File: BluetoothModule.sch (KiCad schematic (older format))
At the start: 13 parts, among them U2 BM83SM1-00TA

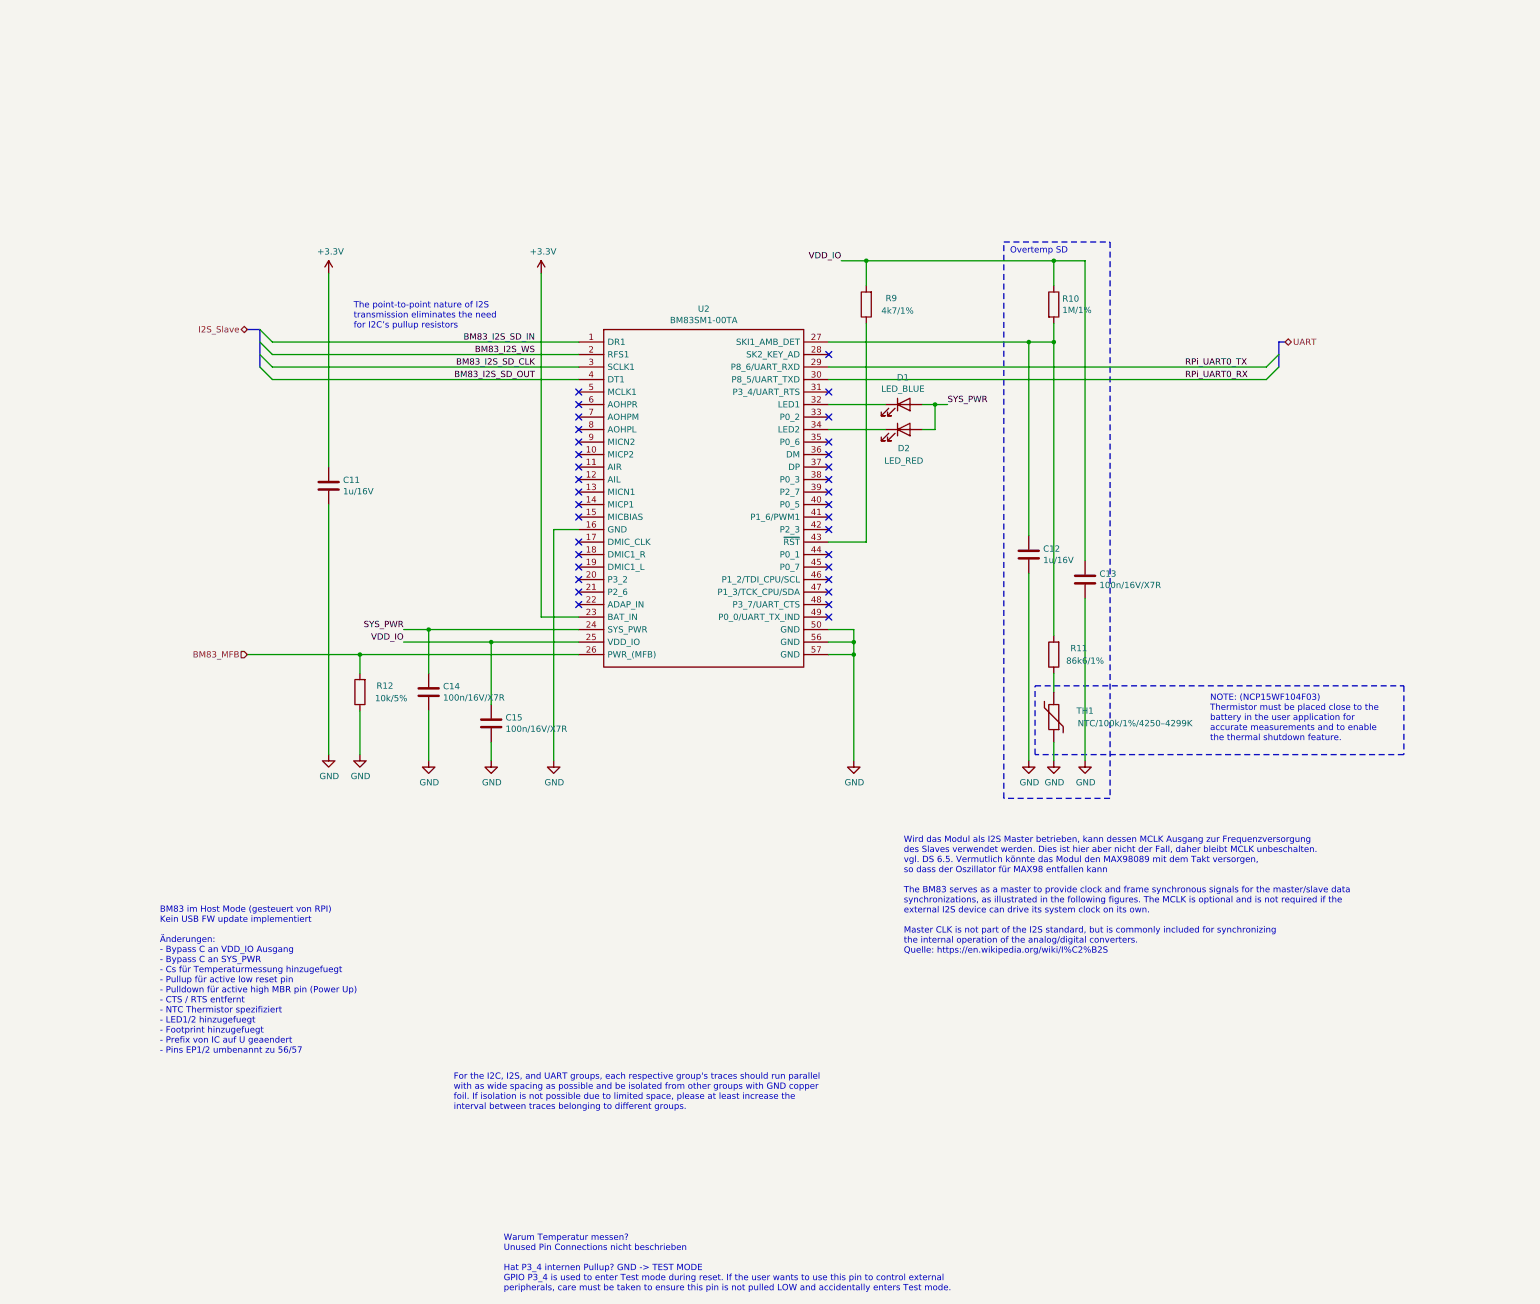
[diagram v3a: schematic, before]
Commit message: - CM3 durch CM4 ersetzt - Spannungsregler für 3,3 und 1,8V entfernt, da nun von CM4 erzeugt - RTC IC getauscht
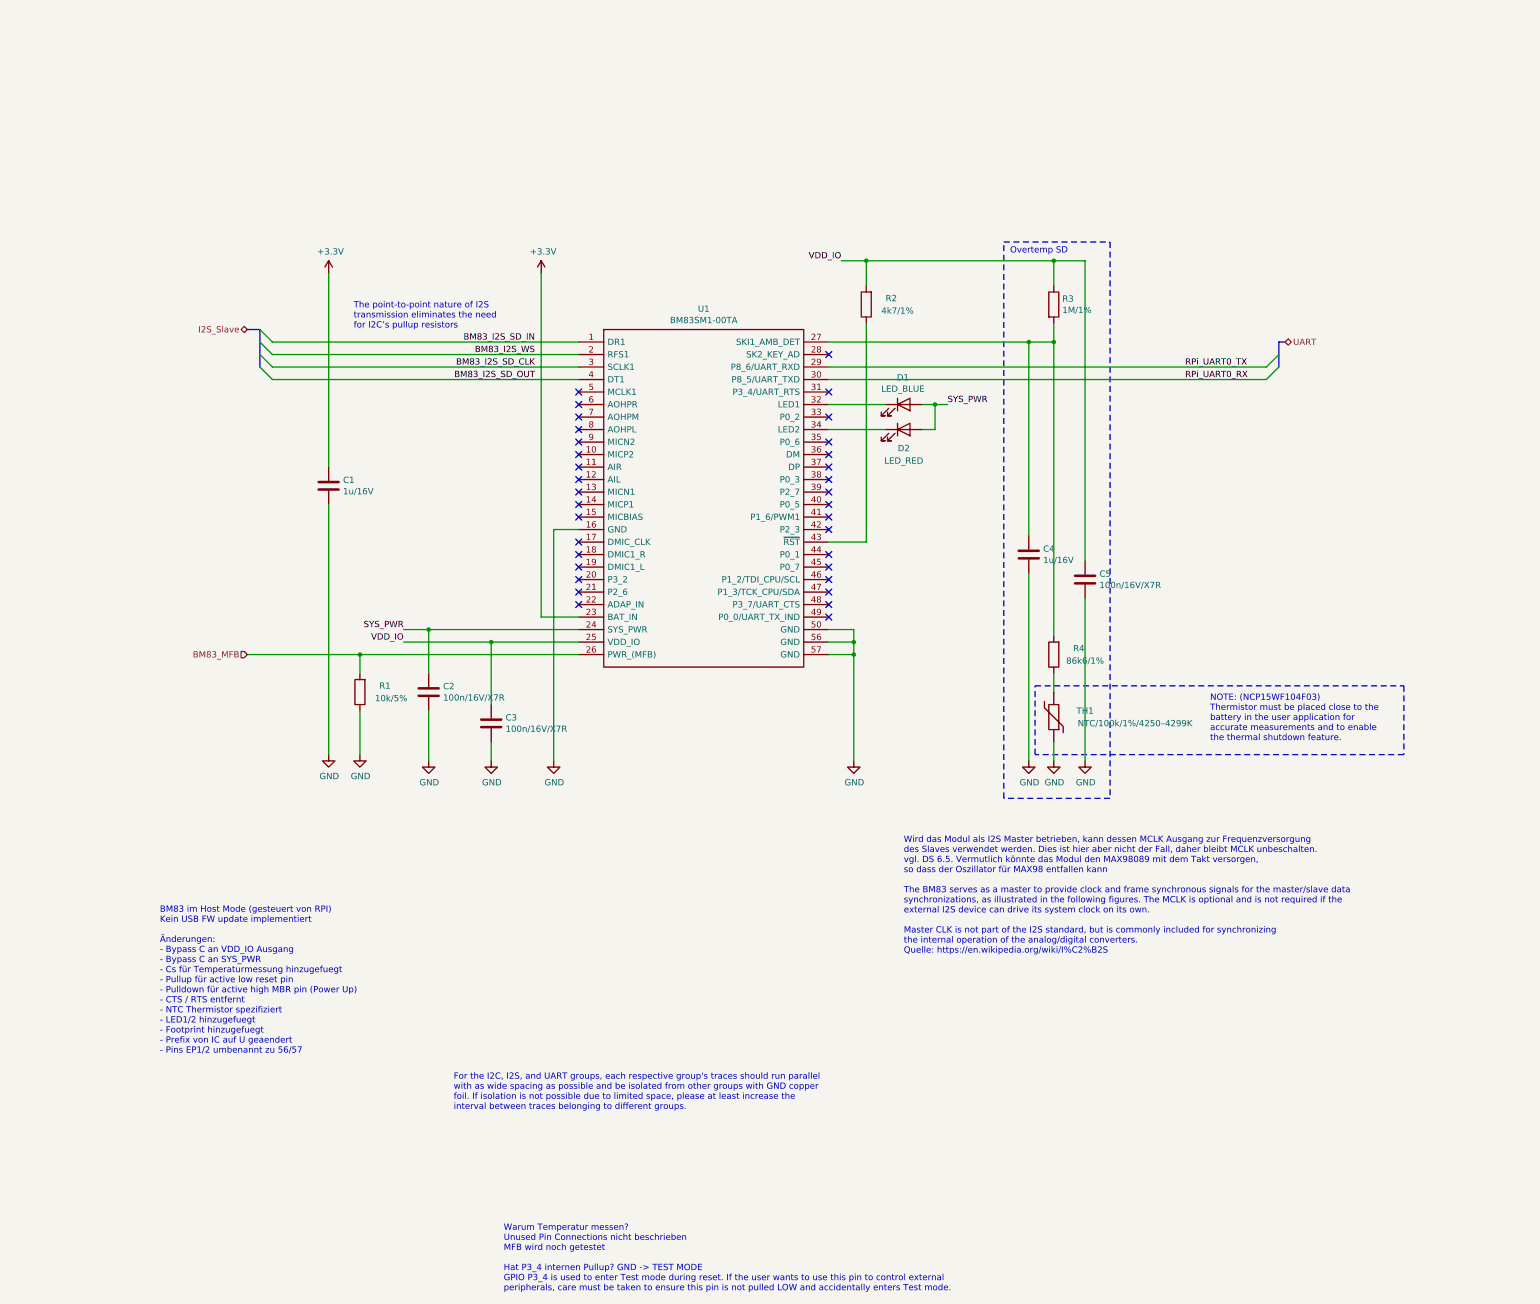
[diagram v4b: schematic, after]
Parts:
- renumbered C11 to C1, C14 to C2, C15 to C3, C12 to C4, C13 to C5, R12 to R1, R9 to R2, R10 to R3, R11 to R4, U2 to U1
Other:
- note added: "Warum Temperatur messen?\nUnused Pin Connections nicht beschrieben\nMFB wird noch getestet\n\nHat P3_4 internen Pullup? GND -> TEST MODE\nGPIO P3_4 is used to enter Test mode during reset. If the user wants to use this pin to control external\nperipherals, care must be taken to ensure this pin is not pulled LOW and accidentally enters Test mode."
- note removed: "Warum Temperatur messen?\nUnused Pin Connections nicht beschrieben\n\nHat P3_4 internen Pullup? GND -> TEST MODE\nGPIO P3_4 is used to enter Test mode during reset. If the user wants to use this pin to control external\nperipherals, care must be taken to ensure this pin is not pulled LOW and accidentally enters Test mode."
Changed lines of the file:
@@
 $Descr A4 11693 8268
 encoding utf-8
-Sheet 3 7
+Sheet 2 8
 Title ""
 Date ""
@@
 BM83_I2S_SD_CLK
 $Comp
-L TeKaDe:BM83SM1-00TA U2
+L TeKaDe:BM83SM1-00TA U1
 U 1 1 620D3641
 P 4400 1450
-F 0 "U2" H 5400 1715 50  0000 C CNN
+F 0 "U1" H 5400 1715 50  0000 C CNN
 F 1 "BM83SM1-00TA" H 5400 1624 50  0000 C CNN
 F 2 "TeKaDe:BM83SM1" H 6250 1550 50  0001 L CNN
@@
 NoConn ~ 4400 3550
 $Comp
-L power:+3.3V #PWR052
+L power:+3.3V #PWR014
 U 1 1 620D3663
 P 4100 900
-F 0 "#PWR052" H 4100 750 50  0001 C CNN
+F 0 "#PWR014" H 4100 750 50  0001 C CNN
 F 1 "+3.3V" H 4115 1073 50  0000 C CNN
 F 2 "" H 4100 900 50  0001 C CNN
@@
 $EndComp
 $Comp
-L Device:C C11
+L Device:C C1
 U 1 1 620D366F
 P 2400 2600
-F 0 "C11" H 2515 2646 50  0000 L CNN
+F 0 "C1" H 2515 2646 50  0000 L CNN
 F 1 "1u/16V" H 2515 2555 50  0000 L CNN
 F 2 "Capacitor_SMD:C_0603_1608Metric" H 2438 2450 50  0001 C CNN
@@
 NoConn ~ 6400 3650
 $Comp
-L power:GND #PWR057
+L power:GND #PWR015
 U 1 1 620E43D7
 P 4200 4800
-F 0 "#PWR057" H 4200 4550 50  0001 C CNN
+F 0 "#PWR015" H 4200 4550 50  0001 C CNN
 F 1 "GND" H 4205 4627 50  0000 C CNN
 F 2 "" H 4200 4800 50  0001 C CNN
@@
 	4200 2950 4400 2950
 $Comp
-L power:GND #PWR058
+L power:GND #PWR016
 U 1 1 620E7F5A
 P 6600 4800
-F 0 "#PWR058" H 6600 4550 50  0001 C CNN
+F 0 "#PWR016" H 6600 4550 50  0001 C CNN
 F 1 "GND" H 6605 4627 50  0000 C CNN
 F 2 "" H 6600 4800 50  0001 C CNN
@@
 $EndComp
 $Comp
-L power:GND #PWR053
+L power:GND #PWR010
 U 1 1 620F327C
 P 2400 4750
-F 0 "#PWR053" H 2400 4500 50  0001 C CNN
+F 0 "#PWR010" H 2400 4500 50  0001 C CNN
 F 1 "GND" H 2405 4577 50  0000 C CNN
 F 2 "" H 2400 4750 50  0001 C CNN
@@
 	2400 4750 2400 2750
 $Comp
-L power:+3.3V #PWR051
+L power:+3.3V #PWR09
 U 1 1 620F6127
 P 2400 900
-F 0 "#PWR051" H 2400 750 50  0001 C CNN
+F 0 "#PWR09" H 2400 750 50  0001 C CNN
 F 1 "+3.3V" H 2415 1073 50  0000 C CNN
 F 2 "" H 2400 900 50  0001 C CNN
@@
 $EndBitmap
 $Comp
-L Device:C C15
+L Device:C C3
 U 1 1 60DA1121
 P 3700 4500
-F 0 "C15" H 3815 4546 50  0000 L CNN
+F 0 "C3" H 3815 4546 50  0000 L CNN
 F 1 "100n/16V/X7R" H 3815 4455 50  0000 L CNN
 F 2 "Capacitor_SMD:C_0603_1608Metric" H 3738 4350 50  0001 C CNN
@@
 $EndComp
 $Comp
-L power:GND #PWR056
+L power:GND #PWR013
 U 1 1 60DA112B
 P 3700 4800
-F 0 "#PWR056" H 3700 4550 50  0001 C CNN
+F 0 "#PWR013" H 3700 4550 50  0001 C CNN
 F 1 "GND" H 3705 4627 50  0000 C CNN
 F 2 "" H 3700 4800 50  0001 C CNN
@@
 	3700 3850 3700 4350
 $Comp
-L Device:C C14
+L Device:C C2
 U 1 1 60DA7A8D
 P 3200 4250
-F 0 "C14" H 3315 4296 50  0000 L CNN
+F 0 "C2" H 3315 4296 50  0000 L CNN
 F 1 "100n/16V/X7R" H 3315 4205 50  0000 L CNN
 F 2 "Capacitor_SMD:C_0603_1608Metric" H 3238 4100 50  0001 C CNN
@@
 $EndComp
 $Comp
-L power:GND #PWR055
+L power:GND #PWR012
 U 1 1 60DA7A97
 P 3200 4800
-F 0 "#PWR055" H 3200 4550 50  0001 C CNN
+F 0 "#PWR012" H 3200 4550 50  0001 C CNN
 F 1 "GND" H 3205 4627 50  0000 C CNN
 F 2 "" H 3200 4800 50  0001 C CNN
@@
 Wird das Modul als I2S Master betrieben, kann dessen MCLK Ausgang zur Frequenzversorgung \ndes Slaves verwendet werden. Dies ist hier aber nicht der Fall, daher bleibt MCLK unbeschalten.\nvgl. DS 6.5. Vermutlich könnte das Modul den MAX98089 mit dem Takt versorgen, \nso dass der Oszillator für MAX98 entfallen kann\n\nThe BM83 serves as a master to provide clock and frame synchronous signals for the master/slave data\nsynchronizations, as illustrated in the following figures. The MCLK is optional and is not required if the\nexternal I2S device can drive its system clock on its own.\n\nMaster CLK is not part of the I2S standard, but is commonly included for synchronizing \nthe internal operation of the analog/digital converters.\nQuelle: https://en.wikipedia.org/wiki/I%C2%B2S
 $Comp
-L Device:R R9
+L Device:R R2
 U 1 1 60DB214B
 P 6700 1150
-F 0 "R9" H 6500 1100 50  0000 C CNN
+F 0 "R2" H 6500 1100 50  0000 C CNN
 F 1 "4k7/1%" H 6450 1200 50  0000 C CNN
 F 2 "Resistor_SMD:R_0603_1608Metric" V 6740 1140 50  0001 C CNN
@@
 Connection ~ 8000 1450
 $Comp
-L power:GND #PWR061
+L power:GND #PWR019
 U 1 1 60DAF699
 P 8450 4800
-F 0 "#PWR061" H 8450 4550 50  0001 C CNN
+F 0 "#PWR019" H 8450 4550 50  0001 C CNN
 F 1 "GND" H 8455 4627 50  0000 C CNN
 F 2 "" H 8450 4800 50  0001 C CNN
@@
 $EndComp
 $Comp
-L power:GND #PWR059
+L power:GND #PWR017
 U 1 1 60DAEFE7
 P 8000 4800
-F 0 "#PWR059" H 8000 4550 50  0001 C CNN
+F 0 "#PWR017" H 8000 4550 50  0001 C CNN
 F 1 "GND" H 8005 4627 50  0000 C CNN
 F 2 "" H 8000 4800 50  0001 C CNN
@@
 $EndComp
 $Comp
-L Device:C C12
+L Device:C C4
 U 1 1 60DAD2BA
 P 8000 3150
-F 0 "C12" H 8115 3196 50  0000 L CNN
+F 0 "C4" H 8115 3196 50  0000 L CNN
 F 1 "1u/16V" H 8115 3105 50  0000 L CNN
 F 2 "Capacitor_SMD:C_0603_1608Metric" H 8038 3000 50  0001 C CNN
@@
 	8200 1450 8200 3800
 $Comp
-L power:GND #PWR060
+L power:GND #PWR018
 U 1 1 60E2C9E3
 P 8200 4800
-F 0 "#PWR060" H 8200 4550 50  0001 C CNN
+F 0 "#PWR018" H 8200 4550 50  0001 C CNN
 F 1 "GND" H 8205 4627 50  0000 C CNN
 F 2 "" H 8200 4800 50  0001 C CNN
@@
 $EndComp
 $Comp
-L Device:R R11
+L Device:R R4
 U 1 1 620D36B1
 P 8200 3950
-F 0 "R11" H 8000 3900 50  0000 C CNN
+F 0 "R4" H 8000 3900 50  0000 C CNN
 F 1 "86k6/1%" H 7950 4000 50  0000 C CNN
 F 2 "Resistor_SMD:R_0603_1608Metric" V 8240 3940 50  0001 C CNN
@@
 RPi_UART0_TX
 $Comp
-L Device:R R10
+L Device:R R3
 U 1 1 620D36AB
 P 8200 1150
-F 0 "R10" H 8268 1196 50  0000 L CNN
+F 0 "R3" H 8268 1196 50  0000 L CNN
 F 1 "1M/1%" H 8268 1105 50  0000 L CNN
 F 2 "Resistor_SMD:R_0603_1608Metric" V 8240 1140 50  0001 C CNN
@@
 	8450 3200 8450 800
 $Comp
-L Device:C C13
+L Device:C C5
 U 1 1 60DADF73
 P 8450 3350
-F 0 "C13" H 8565 3396 50  0000 L CNN
+F 0 "C5" H 8565 3396 50  0000 L CNN
 F 1 "100n/16V/X7R" H 8565 3305 50  0000 L CNN
 F 2 "Capacitor_SMD:C_0603_1608Metric" H 8488 3200 50  0001 C CNN
@@
 $EndComp
 $Comp
-L Device:R R12
+L Device:R R1
 U 1 1 60E6FDE1
 P 2650 4250
-F 0 "R12" H 2450 4200 50  0000 C CNN
+F 0 "R1" H 2450 4200 50  0000 C CNN
 F 1 "10k/5%" H 2400 4300 50  0000 C CNN
 F 2 "Resistor_SMD:R_0603_1608Metric" V 2690 4240 50  0001 C CNN
@@
 $EndComp
 $Comp
-L power:GND #PWR054
+L power:GND #PWR011
 U 1 1 60E7094B
 P 2650 4750
-F 0 "#PWR054" H 2650 4500 50  0001 C CNN
+F 0 "#PWR011" H 2650 4500 50  0001 C CNN
 F 1 "GND" H 2655 4577 50  0000 C CNN
 F 2 "" H 2650 4750 50  0001 C CNN
@@
 NoConn ~ 6400 1850
 Text Notes 3800 9050 0    50   ~ 0
-Warum Temperatur messen?\nUnused Pin Connections nicht beschrieben\n\nHat P3_4 internen Pullup? GND -> TEST MODE\nGPIO P3_4 is used to enter Test mode during reset. If the user wants to use this pin to control external\nperipherals, care must be taken to ensure this pin is not pulled LOW and accidentally enters Test mode.
+Warum Temperatur messen?\nUnused Pin Connections nicht beschrieben\nMFB wird noch getestet\n\nHat P3_4 internen Pullup? GND -> TEST MODE\nGPIO P3_4 is used to enter Test mode during reset. If the user wants to use this pin to control external\nperipherals, care must be taken to ensure this pin is not pulled LOW and accidentally enters Test mode.
 Wire Wire Line
 	3000 3750 3200 3750

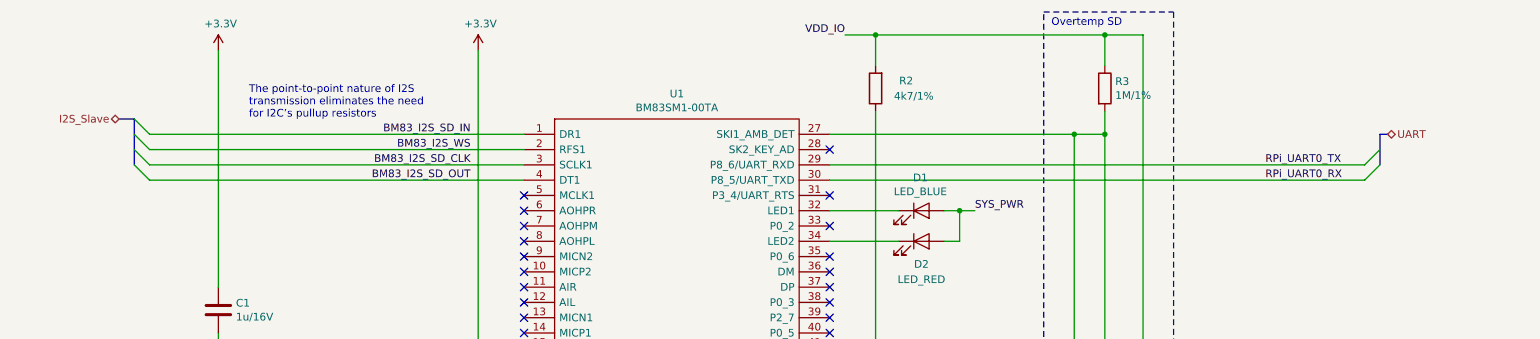
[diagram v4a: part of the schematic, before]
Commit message: - Bus Topologie entfernt - Levelshifter auf eigenes Blatt, abgeschlossen
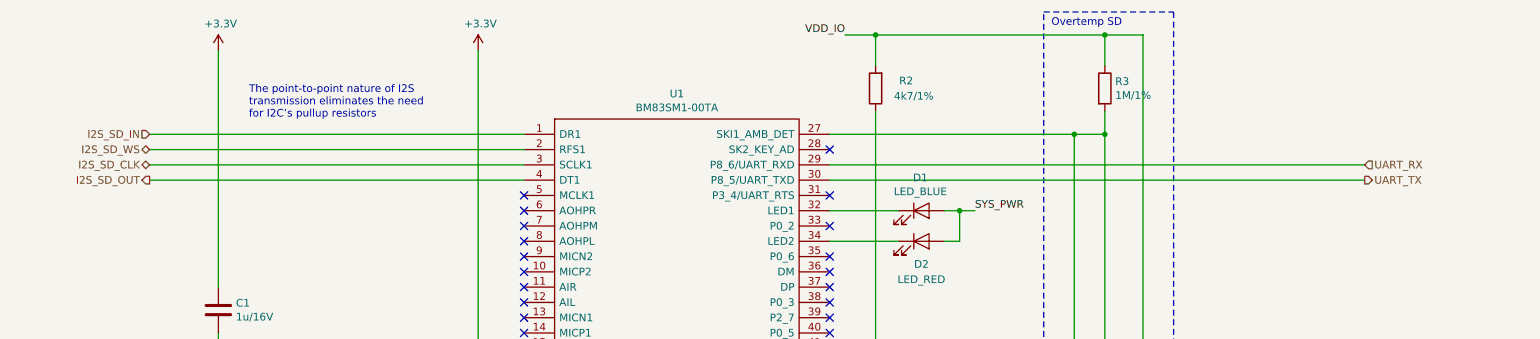
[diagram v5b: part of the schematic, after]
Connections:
- net BM83_I2S_SD_CLK renamed I2S_SD_CLK
- net BM83_I2S_SD_IN renamed I2S_SD_IN
- net BM83_I2S_SD_OUT renamed I2S_SD_OUT
- net BM83_I2S_WS renamed I2S_SD_WS
- net RPi_UART0_RX renamed UART_TX
- net RPi_UART0_TX renamed UART_RX
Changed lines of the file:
@@
 $Descr A4 11693 8268
 encoding utf-8
-Sheet 2 8
+Sheet 7 9
 Title ""
 Date ""
@@
 Comment4 ""
 $EndDescr
-Text Label 4050 1450 2    50   ~ 0
-BM83_I2S_SD_IN
-Text Label 4050 1550 2    50   ~ 0
-BM83_I2S_WS
-Text Label 4050 1650 2    50   ~ 0
-BM83_I2S_SD_CLK
 $Comp
 L TeKaDe:BM83SM1-00TA U1
@@
 Text HLabel 1750 3950 0    50   Input ~ 0
 BM83_MFB
-Text HLabel 10050 1450 2    50   BiDi ~ 0
-UART
-Entry Wire Line
-	9900 1650 10000 1550
-Entry Wire Line
-	9900 1750 10000 1650
-Wire Bus Line
-	10000 1450 10050 1450
+Text HLabel 9900 1650 2    50   Input ~ 0
+UART_RX
 Wire Wire Line
 	6600 3950 6600 4800
@@
 Wire Wire Line
 	3700 3850 4400 3850
-Text Label 4050 1750 2    50   ~ 0
-BM83_I2S_SD_OUT
-Wire Bus Line
-	1850 1350 1750 1350
 Wire Wire Line
 	1950 1750 4400 1750
-Entry Wire Line
-	1850 1650 1950 1750
-Wire Wire Line
-	1950 1650 4400 1650
-Entry Wire Line
-	1850 1550 1950 1650
 Wire Wire Line
 	1950 1550 4400 1550
-Entry Wire Line
-	1850 1450 1950 1550
-Entry Wire Line
-	1850 1350 1950 1450
-Text HLabel 1750 1350 0    50   BiDi ~ 0
-I2S_Slave
+Text HLabel 1950 1450 0    50   Input ~ 0
+I2S_SD_IN
 Text Notes 2600 1350 0    50   ~ 0
 The point-to-point nature of I2S \ntransmission eliminates the need \nfor I2C’s pullup resistors
@@
 Wire Wire Line
 	8200 1300 8200 1450
-Text Label 9250 1750 0    50   ~ 0
-RPi_UART0_RX
-Text Label 9250 1650 0    50   ~ 0
-RPi_UART0_TX
 $Comp
 L Device:R R3
@@
 Wire Notes Line
 	8050 4750 8050 4200
-Wire Bus Line
-	10000 1450 10000 1650
-Wire Bus Line
-	1850 1350 1850 1650
+Text HLabel 9900 1750 2    50   Output ~ 0
+UART_TX
+Text HLabel 1950 1750 0    50   Output ~ 0
+I2S_SD_OUT
+Text HLabel 1950 1650 0    50   BiDi ~ 0
+I2S_SD_CLK
+Text HLabel 1950 1550 0    50   BiDi ~ 0
+I2S_SD_WS
+Wire Wire Line
+	1950 1650 4400 1650
 $EndSCHEMATC
